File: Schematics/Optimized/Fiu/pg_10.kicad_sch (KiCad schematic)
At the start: 74 parts, among them U1101 XBUF64, U1102 XBUF64

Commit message: FIU: integrate entire rotor
Tested: passed run_udiag on r2000
Tested: passed boot_env (fiu-5d8246), until PRETTY_PRINTER exception
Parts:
- added U401: XPAR64, symbol r1000:XPAR64
- added U402: F244, symbol r1000:F244
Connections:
- net F.FIU.P0: now also U402.18 (Y0)
- net F.FIU.P1: now also U402.16 (Y1)
- net F.FIU.P2: now also U402.14 (Y2)
- net F.FIU.P3: now also U402.12 (Y3)
- net F.FIU.P4: now also U402.9 (Y4)
- net F.FIU.P5: now also U402.7 (Y5)
- net F.FIU.P6: now also U402.5 (Y6)
- net F.FIU.P7: now also U402.3 (Y7)
- net FIU_F.OE~: now also U402.1 (OE0), U402.19 (OE1)
- net VO.D0: now also U401.2 (I0)
- net VO.D1: now also U401.3 (I1)
- net VO.D10: now also U401.12 (I10)
- net VO.D11: now also U401.13 (I11)
- net VO.D12: now also U401.14 (I12)
- net VO.D13: now also U401.15 (I13)
- net VO.D14: now also U401.16 (I14)
- net VO.D15: now also U401.17 (I15)
- net VO.D16: now also U401.18 (I16)
- net VO.D17: now also U401.19 (I17)
- net VO.D18: now also U401.20 (I18)
- net VO.D19: now also U401.21 (I19)
- net VO.D2: now also U401.4 (I2)
- net VO.D20: now also U401.22 (I20)
- net VO.D21: now also U401.23 (I21)
- net VO.D22: now also U401.24 (I22)
- net VO.D23: now also U401.25 (I23)
- net VO.D24: now also U401.26 (I24)
- net VO.D25: now also U401.27 (I25)
- net VO.D26: now also U401.28 (I26)
- net VO.D27: now also U401.29 (I27)
- net VO.D28: now also U401.30 (I28)
- net VO.D29: now also U401.31 (I29)
- net VO.D3: now also U401.5 (I3)
- net VO.D30: now also U401.32 (I30)
- net VO.D31: now also U401.33 (I31)
- net VO.D32: now also U401.34 (I32)
- net VO.D33: now also U401.35 (I33)
- net VO.D34: now also U401.36 (I34)
- net VO.D35: now also U401.37 (I35)
- net VO.D36: now also U401.38 (I36)
- net VO.D37: now also U401.39 (I37)
- net VO.D38: now also U401.40 (I38)
- net VO.D39: now also U401.41 (I39)
- net VO.D4: now also U401.6 (I4)
- net VO.D40: now also U401.42 (I40)
- net VO.D41: now also U401.43 (I41)
- net VO.D42: now also U401.44 (I42)
- net VO.D43: now also U401.45 (I43)
- net VO.D44: now also U401.46 (I44)
- net VO.D45: now also U401.47 (I45)
- net VO.D46: now also U401.48 (I46)
- net VO.D47: now also U401.49 (I47)
- net VO.D48: now also U401.50 (I48)
- net VO.D49: now also U401.51 (I49)
- net VO.D5: now also U401.7 (I5)
- net VO.D50: now also U401.52 (I50)
- net VO.D51: now also U401.53 (I51)
- net VO.D52: now also U401.54 (I52)
- net VO.D53: now also U401.55 (I53)
- net VO.D54: now also U401.56 (I54)
- net VO.D55: now also U401.57 (I55)
- net VO.D56: now also U401.58 (I56)
- net VO.D57: now also U401.59 (I57)
- net VO.D58: now also U401.60 (I58)
- net VO.D59: now also U401.61 (I59)
- net VO.D6: now also U401.8 (I6)
- net VO.D60: now also U401.62 (I60)
- net VO.D61: now also U401.63 (I61)
- net VO.D62: now also U401.64 (I62)
- net VO.D63: now also U401.65 (I63)
- net VO.D7: now also U401.9 (I7)
- net VO.D8: now also U401.10 (I8)
- net VO.D9: now also U401.11 (I9)
- new net: U401.70 (P4), U402.11 (I4)
- new net: U401.71 (P5), U402.13 (I5)
- new net: U401.72 (P6), U402.15 (I6)
- new net: U401.73 (P7), U402.17 (I7)
- new net: U401.66 (P0), U402.2 (I0)
- new net: U401.67 (P1), U402.4 (I1)
- new net: U401.68 (P2), U402.6 (I2)
- new net: U401.69 (P3), U402.8 (I3)
- new net DIAG.FPAR: U401.1 (ODD)
- no-connect marks 0 -> 1
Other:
- moved on the sheet: GF103, GF107, GF11, GF111, GF115, GF119, GF123, GF127, GF131, GF135, GF139, GF143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

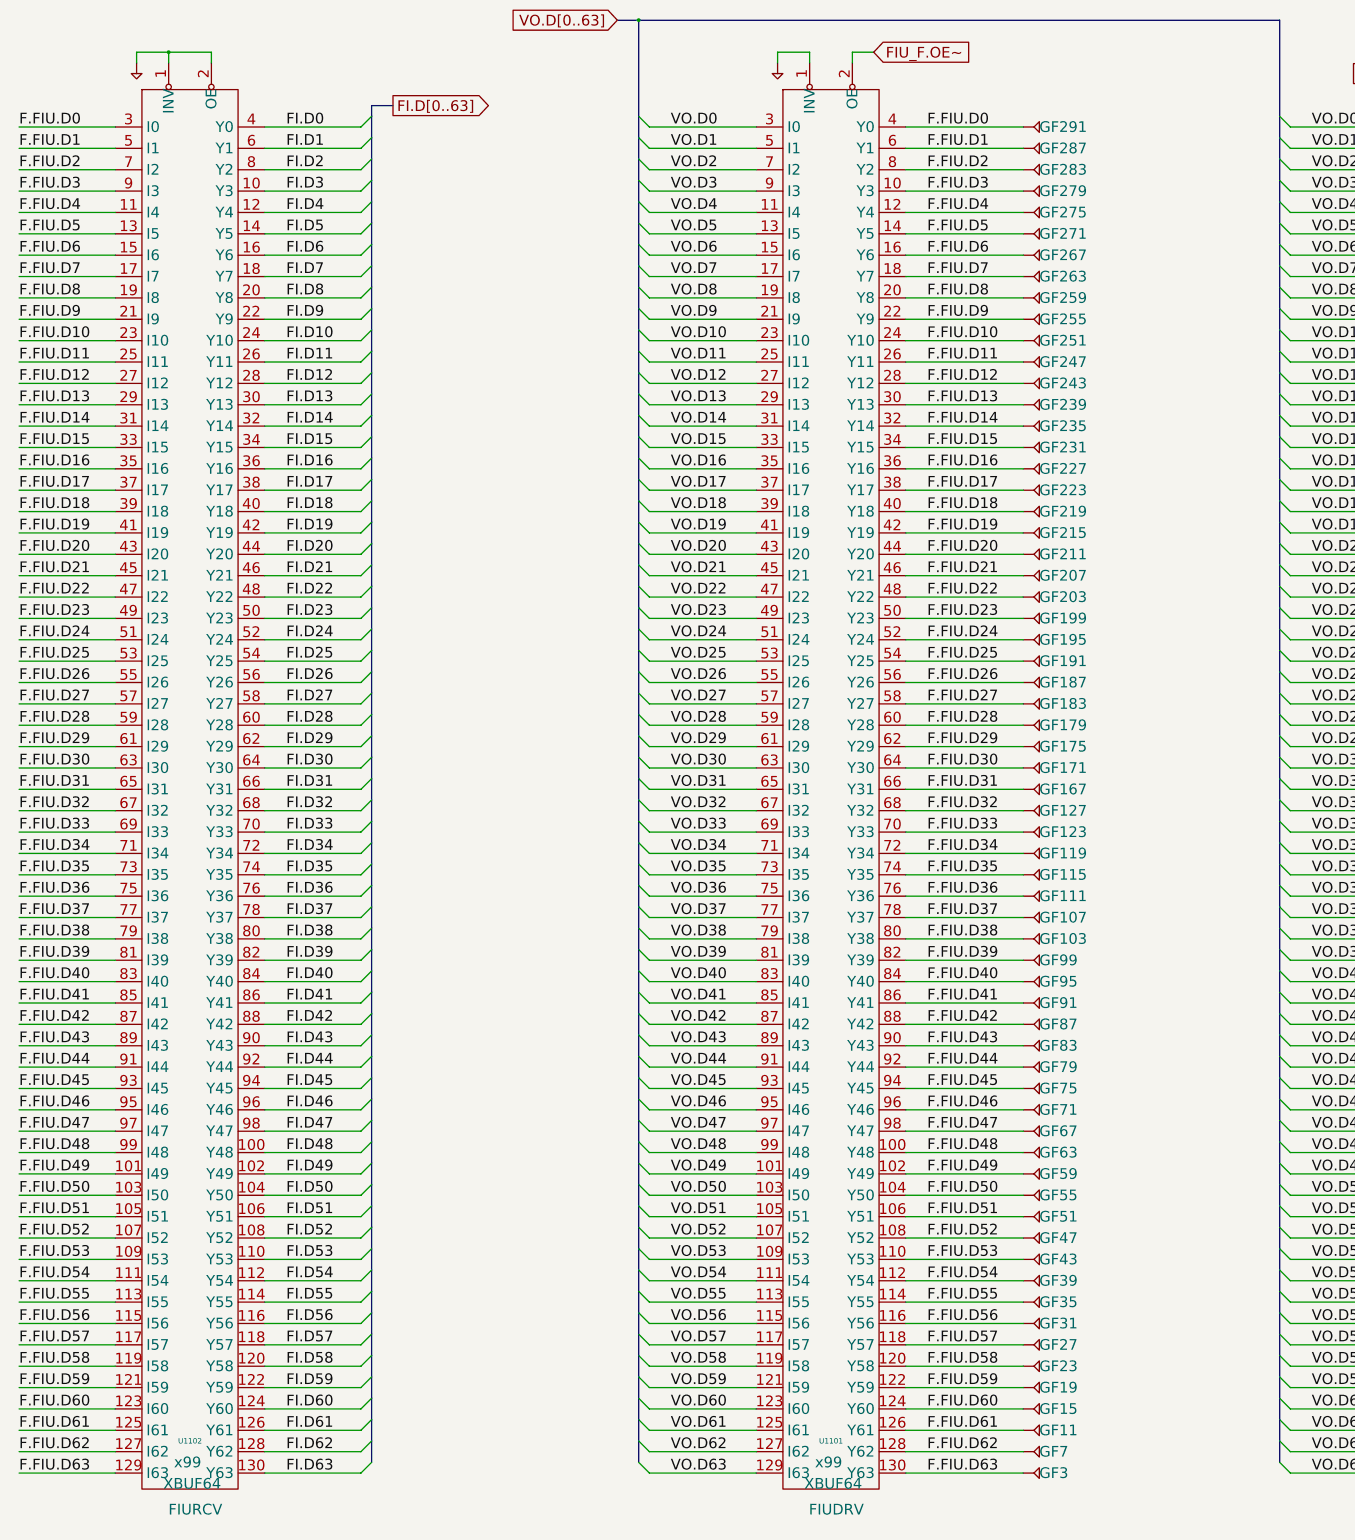
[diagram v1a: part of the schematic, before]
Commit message: Integrate FIU condensations.
NB: Passed PRETTY_PRINTER on pre-integration test-boot
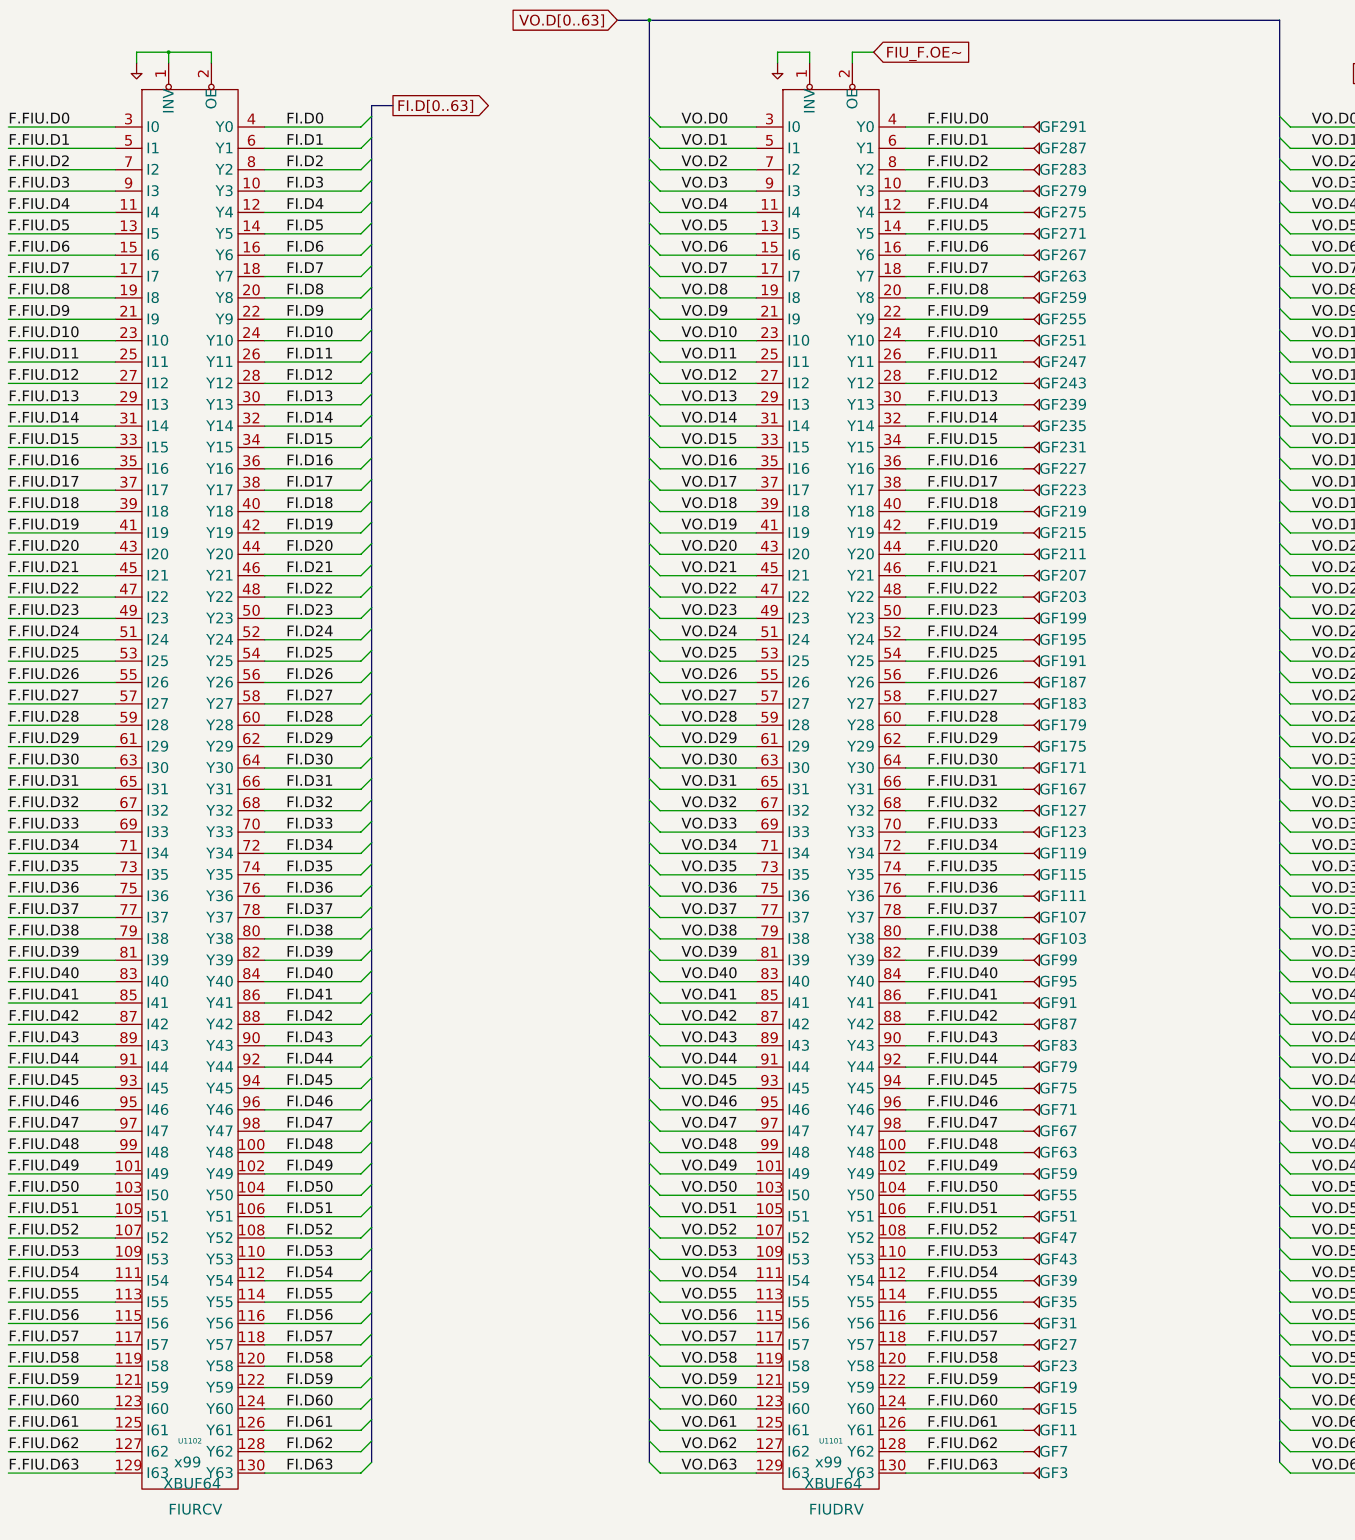
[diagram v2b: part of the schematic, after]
